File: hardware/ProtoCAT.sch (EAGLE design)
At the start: 54 parts, among them U1 ARDUINO, U3 TB6612FNG

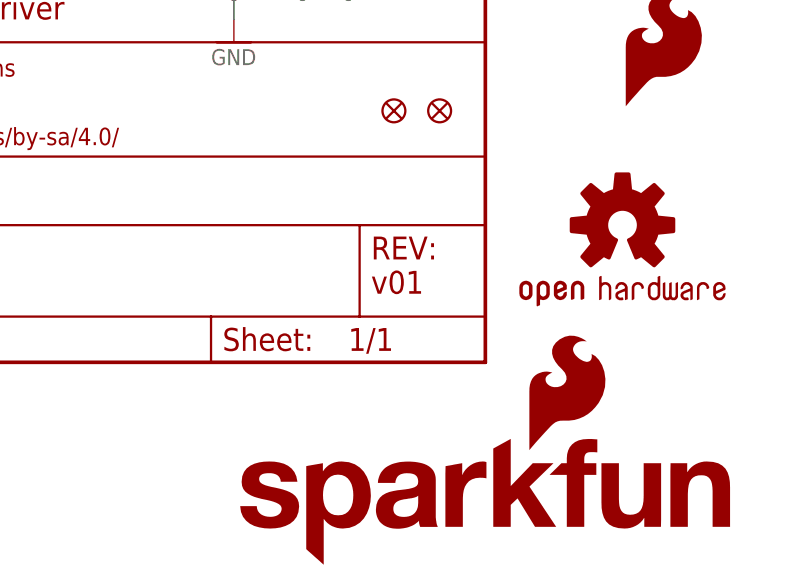
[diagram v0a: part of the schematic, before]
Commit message: Updated Silk and moved Motor connections
Updated the silk name to Ludus ProtoShield and moved the motor
connections below the SMD headers
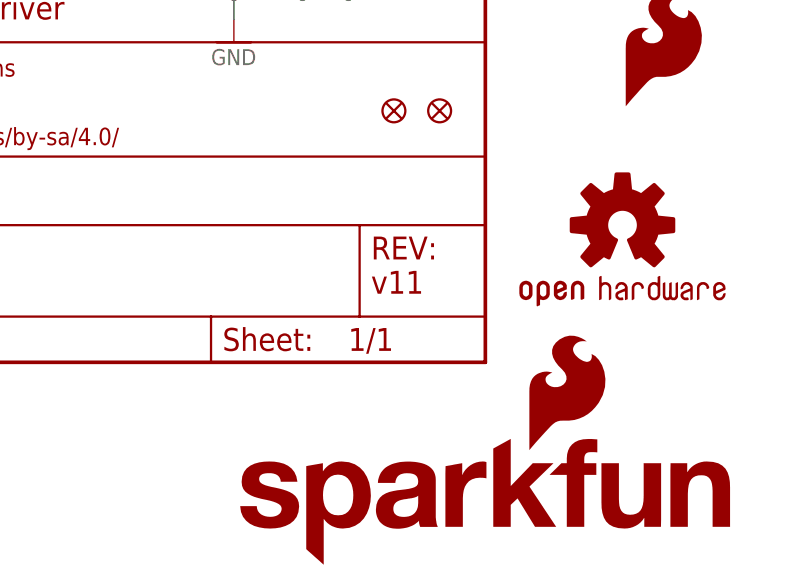
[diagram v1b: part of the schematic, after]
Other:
- note added: "v11"
- note removed: "v01"
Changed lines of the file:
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@@
 <wire x1="116.84" y1="127" x2="116.84" y2="0" width="0.2032" layer="94" style="longdash"/>
 <text x="149.86" y="7.62" size="2.54" layer="94">B. Huang</text>
-<text x="236.22" y="7.62" size="2.54" layer="94">v01</text>
+<text x="236.22" y="7.62" size="2.54" layer="94">v11</text>
 <wire x1="111.76" y1="185.42" x2="111.76" y2="157.48" width="0.1524" layer="94" style="longdash"/>
 <wire x1="111.76" y1="157.48" x2="40.64" y2="157.48" width="0.2032" layer="94" style="longdash"/>
